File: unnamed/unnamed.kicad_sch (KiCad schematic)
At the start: 116 parts, among them J1 Serial, J2 Serial, J3 Conn_01x01_Female, J4 Conn_01x01_Female, J5 S3B-PH-SM4-TB(LF)(SN), J6 S3B-PH-SM4-TB(LF)(SN), SW1 SW_Push, SW10 SW_Push, SW11 SW_Push, SW12 SW_Push, SW13 SW_Push, SW14 SW_Push, SW15 SW_Push, SW16 SW_Push, SW17 SW_Push, SW18 SW_Push, SW19 SW_Push, SW2 SW_Push, SW20 SW_Push, SW21 SW_Push, SW22 SW_Push, SW23 SW_Push, SW24 SW_Push, SW25 SW_SPST, SW26 SW_SPST, SW27 SW_Push, SW28 SW_Push, SW29 SW_Push, SW3 SW_Push, SW30 SW_Push, SW31 SW_Push, SW32 SW_Push, SW33 SW_Push, SW34 SW_Push, SW35 SW_Push, SW36 SW_Push, SW4 SW_Push, SW5 SW_Push, SW6 SW_Push, SW7 SW_Push, SW8 SW_Push, SW9 SW_Push, U1 eliteC, U2 eliteC

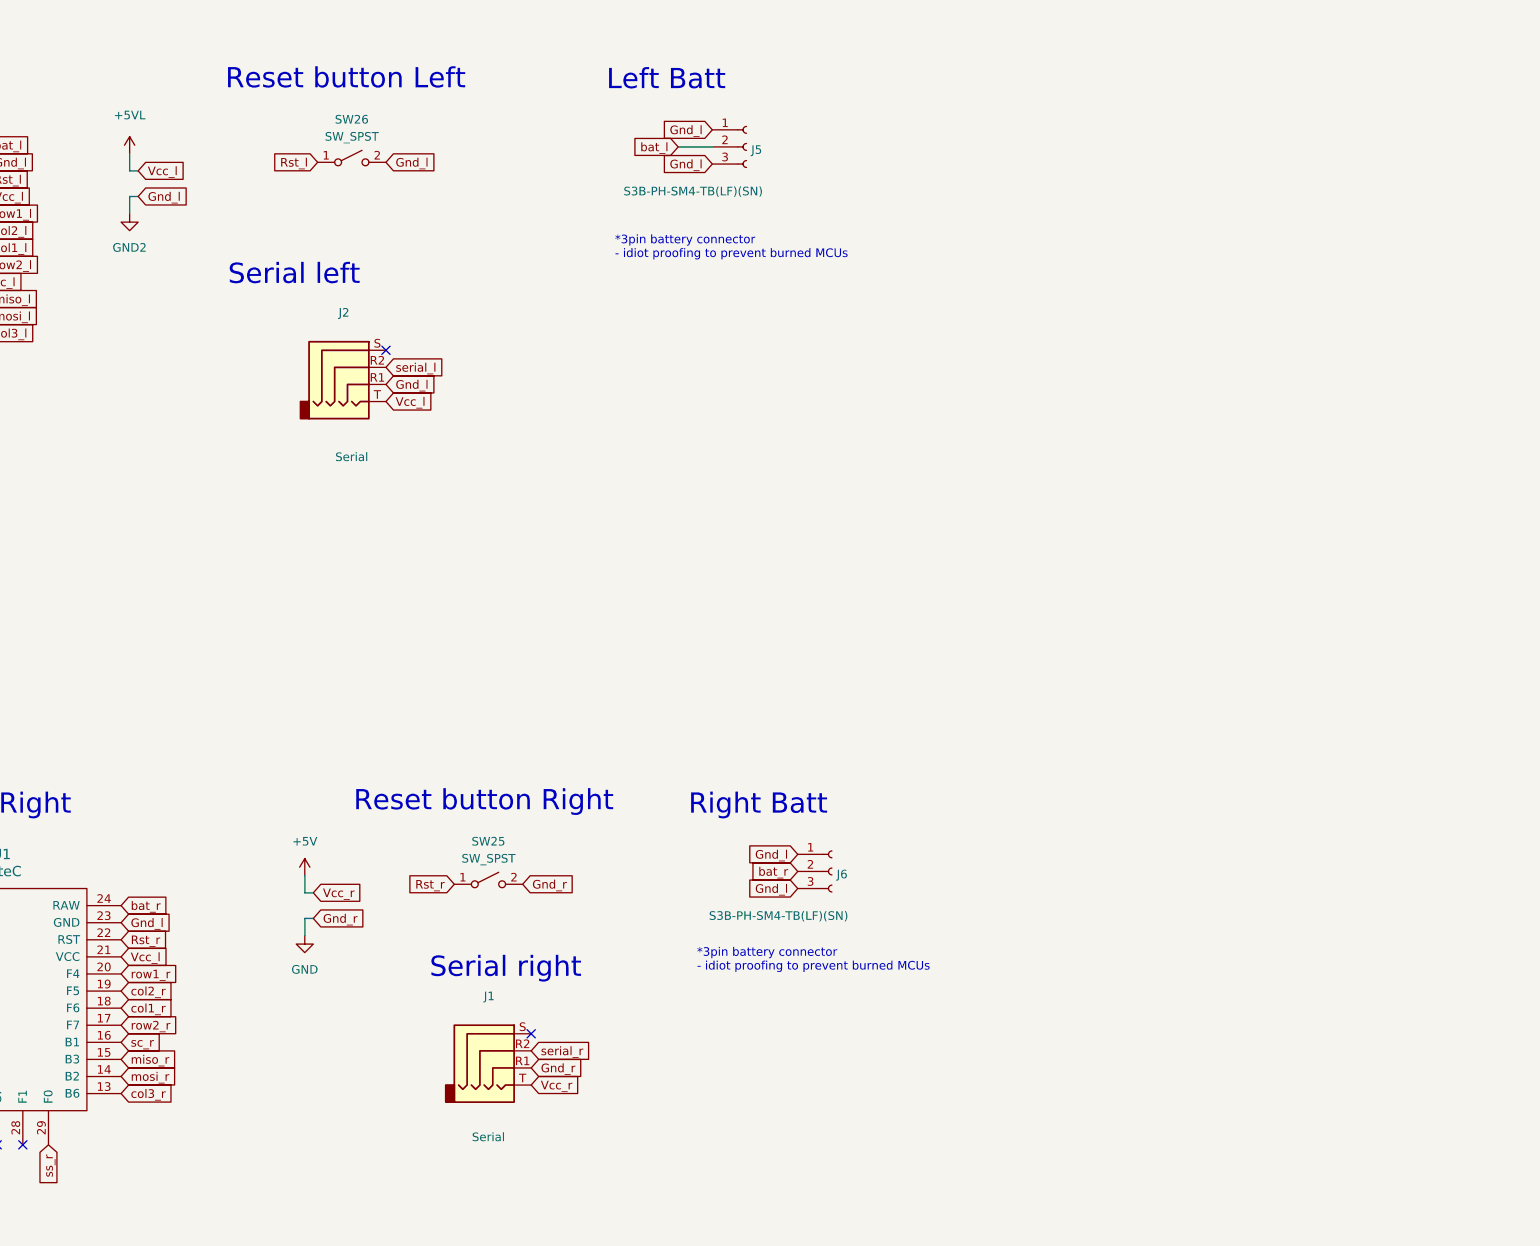
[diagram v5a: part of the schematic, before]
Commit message: Added Cirque FFC connector
Added FFC while prototyping other connection solutions. Need to check how to power Cirque since it's rated up to 3.6v only.
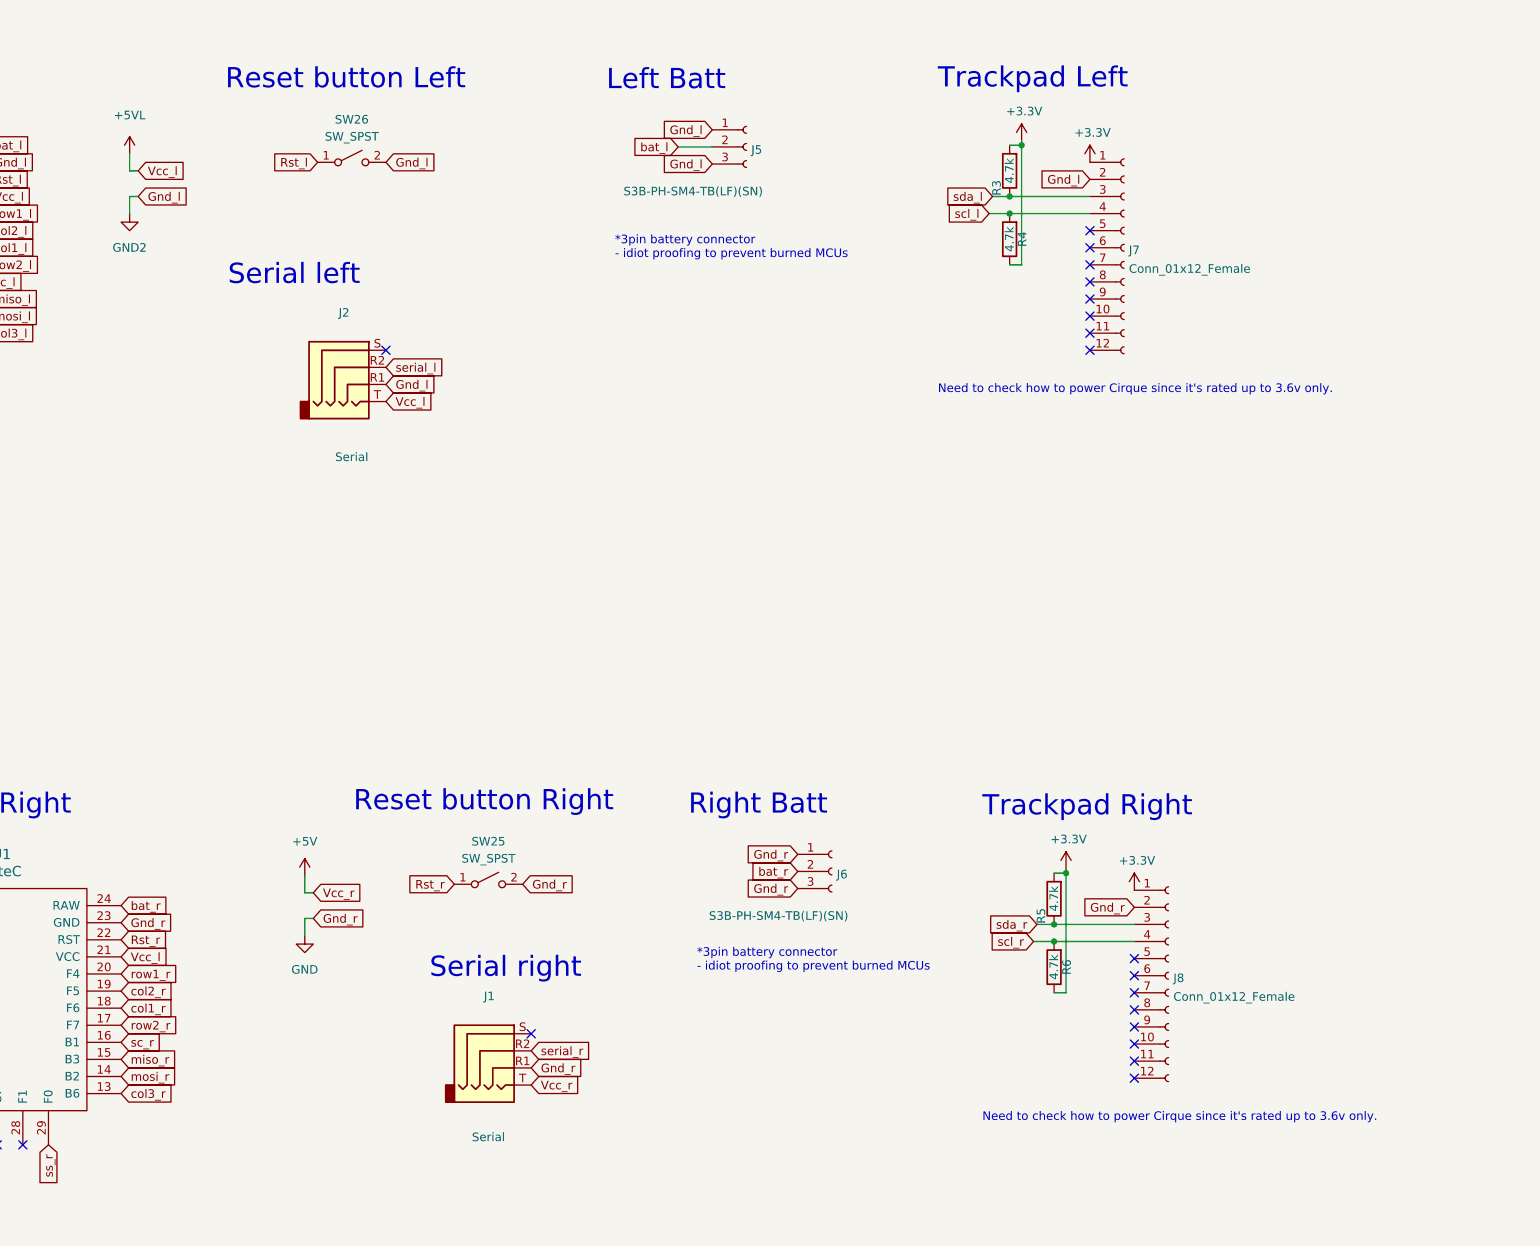
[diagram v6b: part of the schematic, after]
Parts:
- added J7, J8: Conn_01x12_Female, prettylib:FPC-SMD_FH12-12S-0.5SH-55, symbol Connector:Conn_01x12_Female
- added R3, R4, R5, R6: 4.7k, reversible-kicad-footprints:R-0805_2012Metric, symbol Device:R
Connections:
- net GND: now also J6.1 (Pin_1), J6.3 (Pin_3), U1.23 (GND), J8.2 (Pin_2)
- net GND2: now also J7.2 (Pin_2); no longer J6.1 (Pin_1), J6.3 (Pin_3), U1.23 (GND)
- net scl_l: now also J7.4 (Pin_4), R4.2
- net scl_r: now also J8.4 (Pin_4), R6.2
- net sda_l: now also J7.3 (Pin_3), R3.1
- net sda_r: now also J8.3 (Pin_3), R5.1
- new net +3V3: J7.1 (Pin_1), J8.1 (Pin_1), R3.2, R4.1, R5.2, R6.1
- no-connect marks 10 -> 26
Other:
- note added: "Need to check how to power Cirque since it's rated up to 3.6v only."
- note added: "Trackpad Left"
- note added: "Trackpad Right"

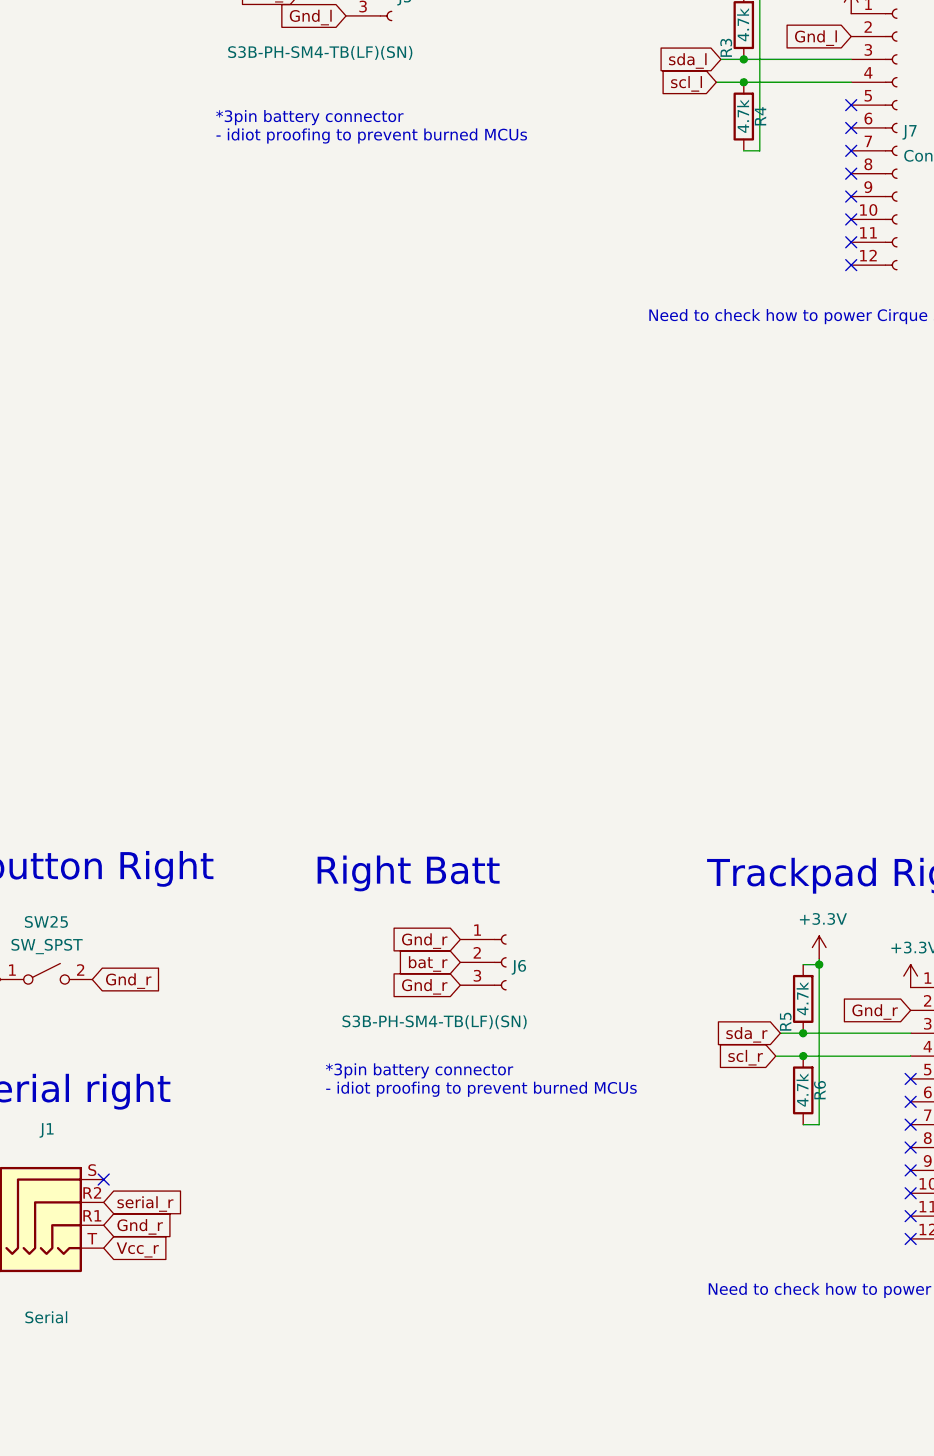
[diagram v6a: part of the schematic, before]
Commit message: Added power switch
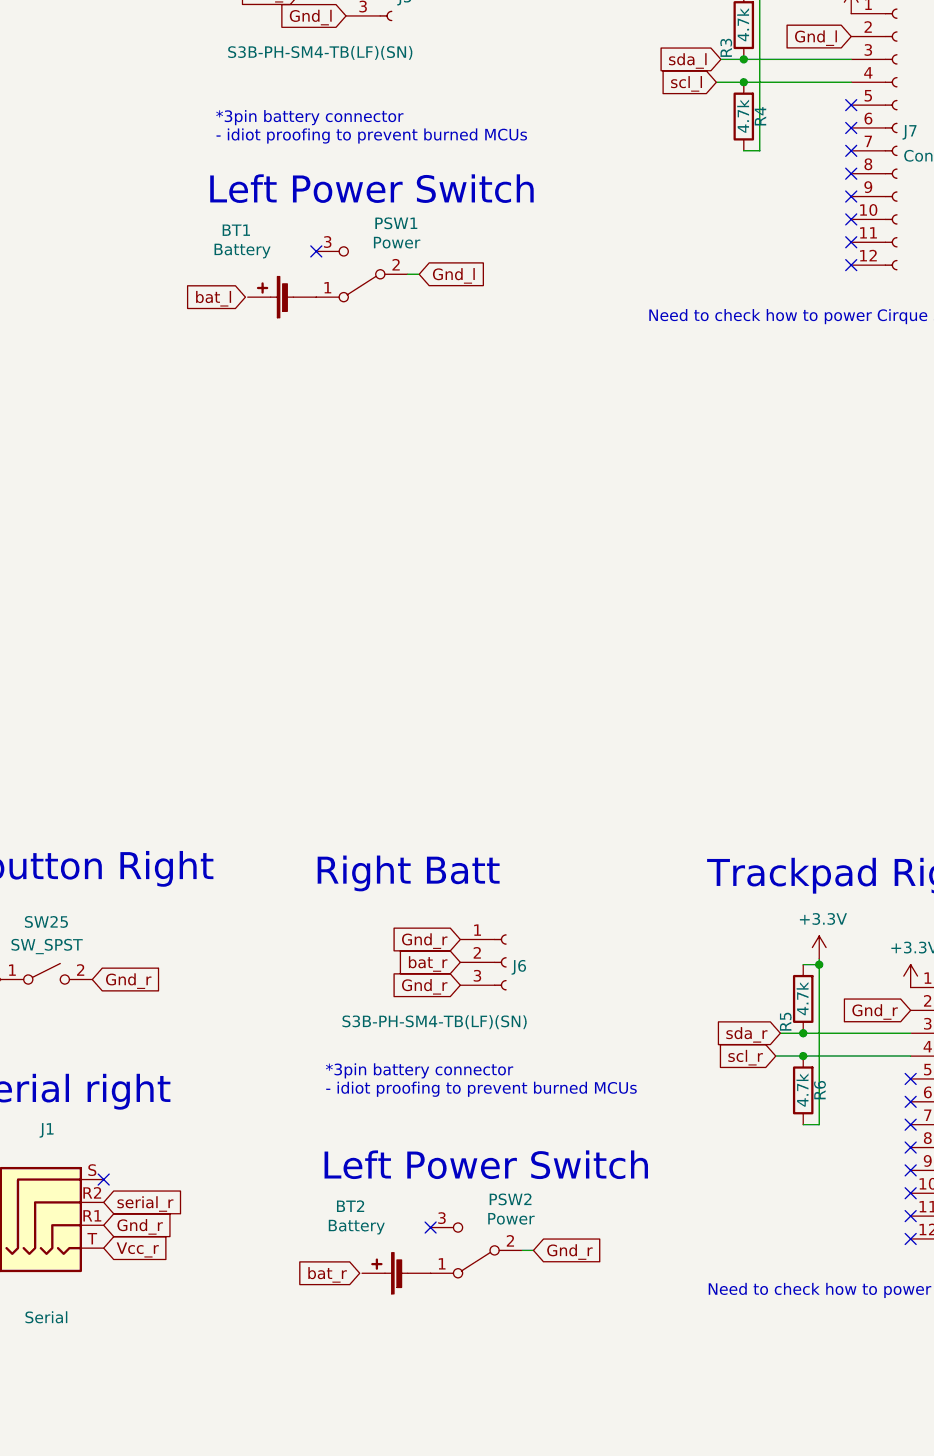
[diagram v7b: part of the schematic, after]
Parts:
- added BT1, BT2: Battery, swoop:Battery_pads_reversible, symbol Device:Battery_Cell
- added PSW1, PSW2: Power, swoop:Power, symbol Switch:SW_SPDT
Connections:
- net GND: now also PSW2.2 (B)
- net GND2: now also PSW1.2 (B)
- new net: BT1.2 (-), PSW1.1 (A)
- new net: BT2.2 (-), PSW2.1 (A)
- no-connect marks 26 -> 28
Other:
- note added: "Left Power Switch"
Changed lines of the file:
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@@
   (no_connect (at 489.712 156.464))
   (no_connect (at 483.108 58.42))
+  (no_connect (at 423.672 64.516))
   (no_connect (at 483.108 48.26))
   (no_connect (at 313.69 184.15))
@@
   (no_connect (at 483.108 50.8))
   (no_connect (at 489.712 164.084))
+  (no_connect (at 436.372 172.974))
   (no_connect (at 489.712 174.244))
   (no_connect (at 483.108 53.34))
@@
     (stroke (width 0) (type default) (color 0 0 0 0))
   )
+  (wire (pts (xy 446.532 175.514) (xy 447.802 175.514))
+    (stroke (width 0) (type default) (color 0 0 0 0))
+  )
   (wire (pts (xy 468.63 43.18) (xy 471.17 43.18))
     (stroke (width 0) (type default) (color 0 0 0 0))
@@
     (stroke (width 0) (type solid) (color 0 0 0 0))
   )
+  (wire (pts (xy 433.832 67.056) (xy 435.102 67.056))
+    (stroke (width 0) (type default) (color 0 0 0 0))
+  )
   (wire (pts (xy 52.07 170.815) (xy 57.15 170.815))
     (stroke (width 0) (type default) (color 0 0 0 0))
@@
     (effects (font (size 1.27 1.27)) (justify right bottom))
   )
+  (text "Left Power Switch" (at 424.18 168.148 0)
+    (effects (font (size 3 3)) (justify left bottom))
+  )
   (text "Need to check how to power Cirque since it's rated up to 3.6v only."
     (at 460.502 72.644 0)
@@
     (effects (font (size 1.27 1.27)) (justify left bottom))
   )
+  (text "Left Power Switch" (at 411.48 59.69 0)
+    (effects (font (size 3 3)) (justify left bottom))
+  )
   (text "Right" (at 22.86 167.005 90)
     (effects (font (size 5 5)) (justify left bottom))
@@
     )
   )
+  (global_label "bat_l" (shape input) (at 415.798 69.596 180)
+    (effects (font (size 1.27 1.27)) (justify right))
+    (property "Intersheet References" "${INTERSHEET_REFS}" (id 0) (at 538.988 200.406 0)
+      (effects (font (size 1.27 1.27)) hide)
+    )
+  )
   (global_label "miso_r" (shape input) (at 339.09 171.45 0)
     (effects (font (size 1.27 1.27)) (justify left))
@@
     )
   )
+  (global_label "bat_r" (shape input) (at 428.498 178.054 180)
+    (effects (font (size 1.27 1.27)) (justify right))
+    (property "Intersheet References" "${INTERSHEET_REFS}" (id 0) (at 551.688 308.864 0)
+      (effects (font (size 1.27 1.27)) hide)
+    )
+  )
+  (global_label "Gnd_r" (shape input) (at 447.802 175.514 0)
+    (effects (font (size 1.27 1.27)) (justify left))
+    (property "Intersheet References" "${INTERSHEET_REFS}" (id 0) (at 324.612 105.664 0)
+      (effects (font (size 1.27 1.27)) hide)
+    )
+  )
   (global_label "col3_r" (shape input) (at 105.41 132.715 90)
     (effects (font (size 1.27 1.27)) (justify left))
@@
     )
   )
+  (global_label "Gnd_l" (shape input) (at 435.102 67.056 0)
+    (effects (font (size 1.27 1.27)) (justify left))
+    (property "Intersheet References" "${INTERSHEET_REFS}" (id 0) (at 311.912 -2.794 0)
+      (effects (font (size 1.27 1.27)) hide)
+    )
+  )
   (global_label "row2_l" (shape input) (at 318.77 53.34 0)
     (effects (font (size 1.27 1.27)) (justify left))
@@
     (pin "2")
   )
+  (symbol (lib_id "Switch:SW_SPDT") (at 428.752 67.056 180) (unit 1)
+    (in_bom yes) (on_board yes)
+    (property "Reference" "PSW1" (id 0) (at 432.562 61.4384 0))
+    (property "Value" "Power" (id 1) (at 432.562 63.5785 0))
+    (property "Footprint" "swoop:Power" (id 2) (at 428.752 67.056 0)
+      (effects (font (size 1.27 1.27)) hide)
+    )
+    (property "Datasheet" "~" (id 3) (at 428.752 67.056 0)
+      (effects (font (size 1.27 1.27)) hide)
+    )
+    (pin "1")
+    (pin "2")
+    (pin "3")
+  )
+  (symbol (lib_id "Device:Battery_Cell") (at 433.832 178.054 90) (unit 1)
+    (in_bom yes) (on_board yes)
+    (property "Reference" "BT2" (id 0) (at 427.482 170.6584 90))
+    (property "Value" "Battery" (id 1) (at 428.117 172.7985 90))
+    (property "Footprint" "swoop:Battery_pads_reversible" (id 2) (at 432.308 178.054 90)
+      (effects (font (size 1.27 1.27)) hide)
+    )
+    (property "Datasheet" "~" (id 3) (at 432.308 178.054 90)
+      (effects (font (size 1.27 1.27)) hide)
+    )
+    (pin "1")
+    (pin "2")
+  )
   (symbol (lib_id "Device:R") (at 471.17 39.37 180) (unit 1)
     (in_bom yes) (on_board yes)
@@
     (pin "2")
   )
+  (symbol (lib_id "Device:Battery_Cell") (at 421.132 69.596 90) (unit 1)
+    (in_bom yes) (on_board yes)
+    (property "Reference" "BT1" (id 0) (at 414.782 62.2004 90))
+    (property "Value" "Battery" (id 1) (at 415.417 64.3405 90))
+    (property "Footprint" "swoop:Battery_pads_reversible" (id 2) (at 419.608 69.596 90)
+      (effects (font (size 1.27 1.27)) hide)
+    )
+    (property "Datasheet" "~" (id 3) (at 419.608 69.596 90)
+      (effects (font (size 1.27 1.27)) hide)
+    )
+    (pin "1")
+    (pin "2")
+  )
   (symbol (lib_id "Switch:SW_Push") (at 217.17 46.99 0) (unit 1)
     (in_bom yes) (on_board yes)
@@
     (pin "4")
   )
+  (symbol (lib_id "Switch:SW_SPDT") (at 441.452 175.514 180) (unit 1)
+    (in_bom yes) (on_board yes)
+    (property "Reference" "PSW2" (id 0) (at 445.262 169.8964 0))
+    (property "Value" "Power" (id 1) (at 445.262 172.0365 0))
+    (property "Footprint" "swoop:Power" (id 2) (at 441.452 175.514 0)
+      (effects (font (size 1.27 1.27)) hide)
+    )
+    (property "Datasheet" "~" (id 3) (at 441.452 175.514 0)
+      (effects (font (size 1.27 1.27)) hide)
+    )
+    (pin "1")
+    (pin "2")
+    (pin "3")
+  )
   (symbol (lib_id "Switch:SW_Push") (at 114.3 58.42 0) (unit 1)
     (in_bom yes) (on_board yes)
@@
       (reference "#PWR0102") (unit 1) (value "GND2") (footprint "")
     )
+    (path "/9e8006cb-49f0-44ed-b39a-9f9d999f305f"
+      (reference "BT1") (unit 1) (value "Battery") (footprint "swoop:Battery_pads_reversible")
+    )
+    (path "/49ecdbf6-deff-4864-ac64-73e23988717d"
+      (reference "BT2") (unit 1) (value "Battery") (footprint "swoop:Battery_pads_reversible")
+    )
     (path "/1a1ab757-51de-4969-8924-8675206b3aa2"
       (reference "C1") (unit 1) (value "C") (footprint "")
@@
       (reference "J8") (unit 1) (value "Conn_01x12_Female") (footprint "prettylib:FPC-SMD_FH12-12S-0.5SH-55")
     )
+    (path "/490427c5-7c38-4754-bcb1-0cc9dfe9dad4"
+      (reference "PSW1") (unit 1) (value "Power") (footprint "swoop:Power")
+    )
+    (path "/a9334cf2-1640-43e7-b224-0fba58d05425"
+      (reference "PSW2") (unit 1) (value "Power") (footprint "swoop:Power")
+    )
     (path "/74b3aa64-9363-448b-93d6-0b22421aa5c3"
